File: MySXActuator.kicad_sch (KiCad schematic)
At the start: 32 parts, among them J1 8P8C, Q1 2N7002, Q2 IRF540N, Q3 IRF540N, Q4 2N7002

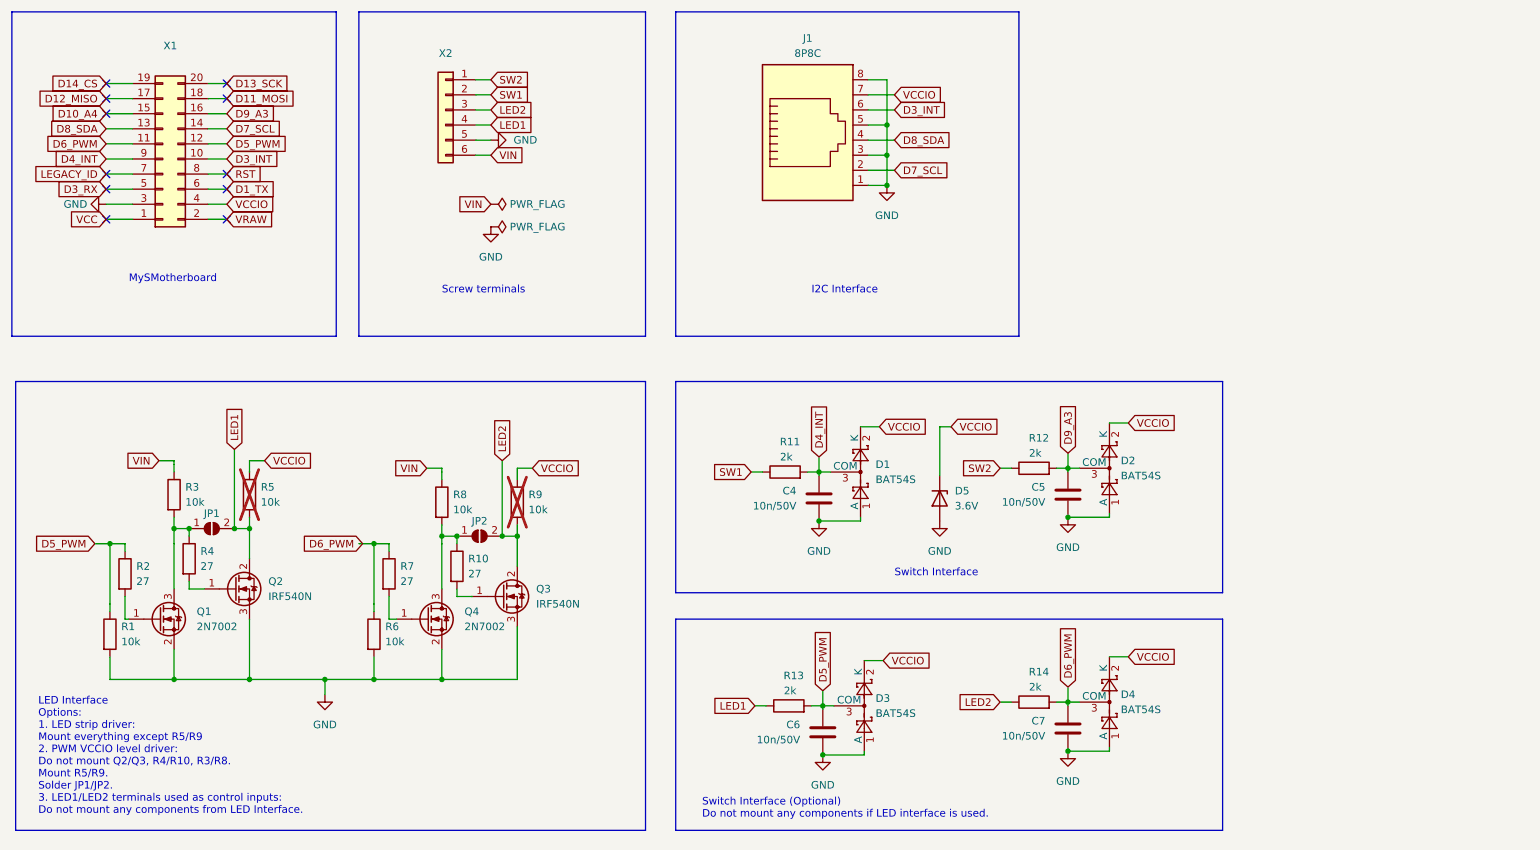
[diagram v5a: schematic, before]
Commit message: Add removed buck converter
- previously removed buck converter is needed to not require power from
RS485 line
- position RJ45 connector closer to center of the board to allow use
straigth connector (facing up)
- replace THT power transistors with SMT power transistors
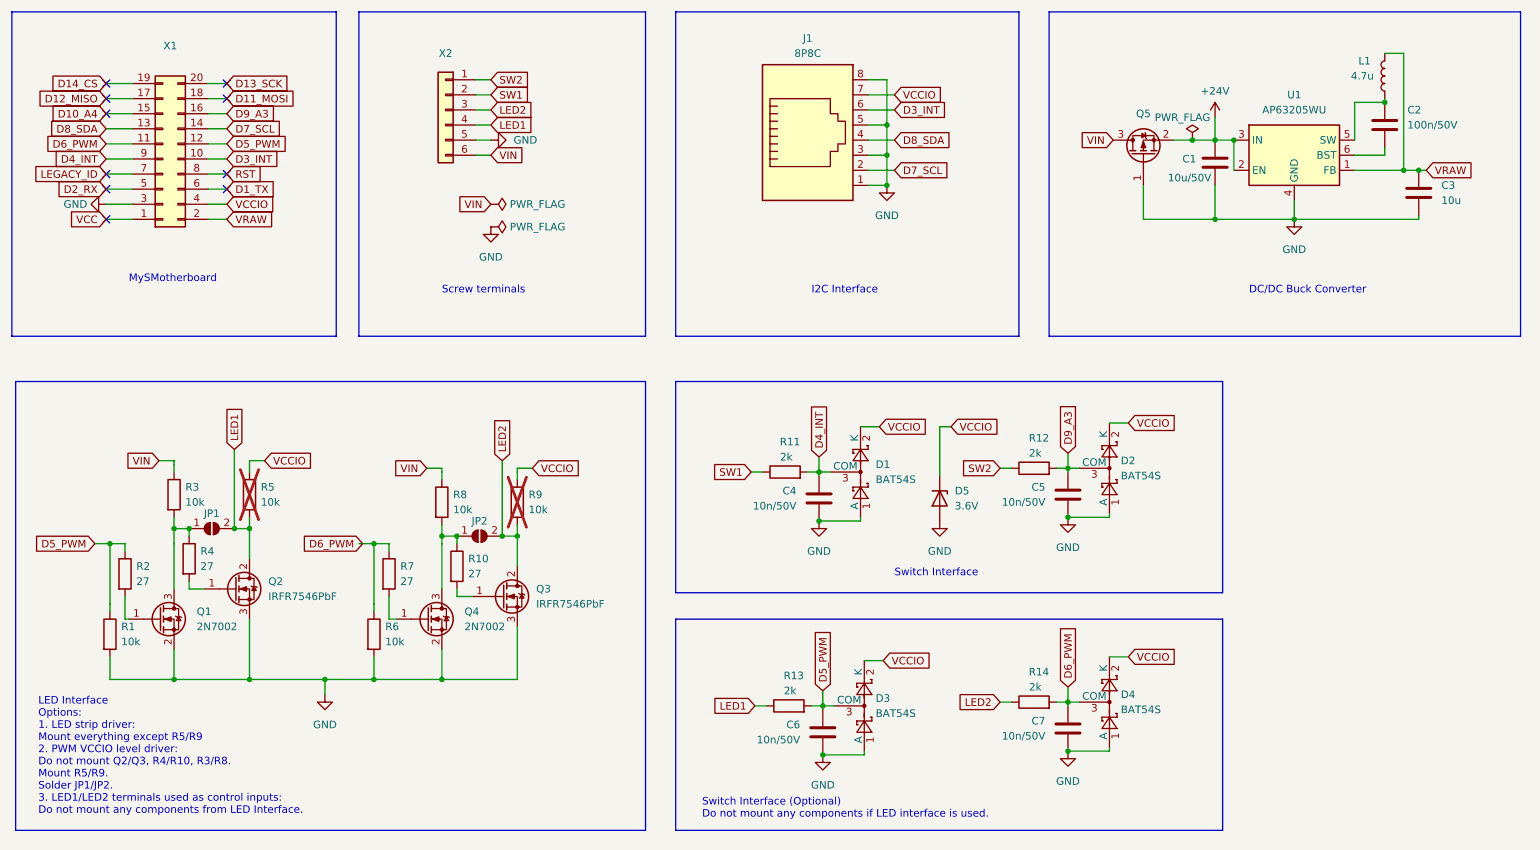
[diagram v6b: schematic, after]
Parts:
- added C1: 10u/50V, Capacitor_SMD:C_1206_3216Metric, symbol Device:C
- added C2: 100n/50V, Capacitor_SMD:C_0402_1005Metric_Pad0.74x0.62mm_HandSolder, symbol Device:C
- added C3: 10u, Capacitor_SMD:C_1206_3216Metric, symbol Device:C
- added L1: 4.7u, Inductor_SMD:L_1210_3225Metric, symbol Device:L
- added Q5: ~, Package_TO_SOT_SMD:SOT-23, symbol Device:Q_PMOS_GSD
- added U1: AP63205WU, Package_TO_SOT_SMD:TSOT-23-6, symbol Regulator_Switching:AP63205WU
- Q2, Q3: value IRF540N -> IRFR7546PbF; footprint Package_TO_SOT_THT:TO-220-3_Vertical -> Package_TO_SOT_SMD:TO-252-2
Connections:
- net GND: now also C1.2, C3.2, Q5.1 (G), U1.4 (GND)
- net VIN: now also Q5.3 (D)
- net VRAW: now also C3.1, L1.2, U1.1 (FB)
- net D3_RX renamed D2_RX
- new net: C2.2, L1.1, U1.5 (SW)
- new net: C2.1, U1.6 (BST)
- new net +24V: C1.1, Q5.2 (S), U1.2 (EN), U1.3 (IN)
- no-connect marks 11 -> 10
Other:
- note added: "DC/DC Buck Converter"
